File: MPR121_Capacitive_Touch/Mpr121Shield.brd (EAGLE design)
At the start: 39 x 28.7 mm, 13 parts

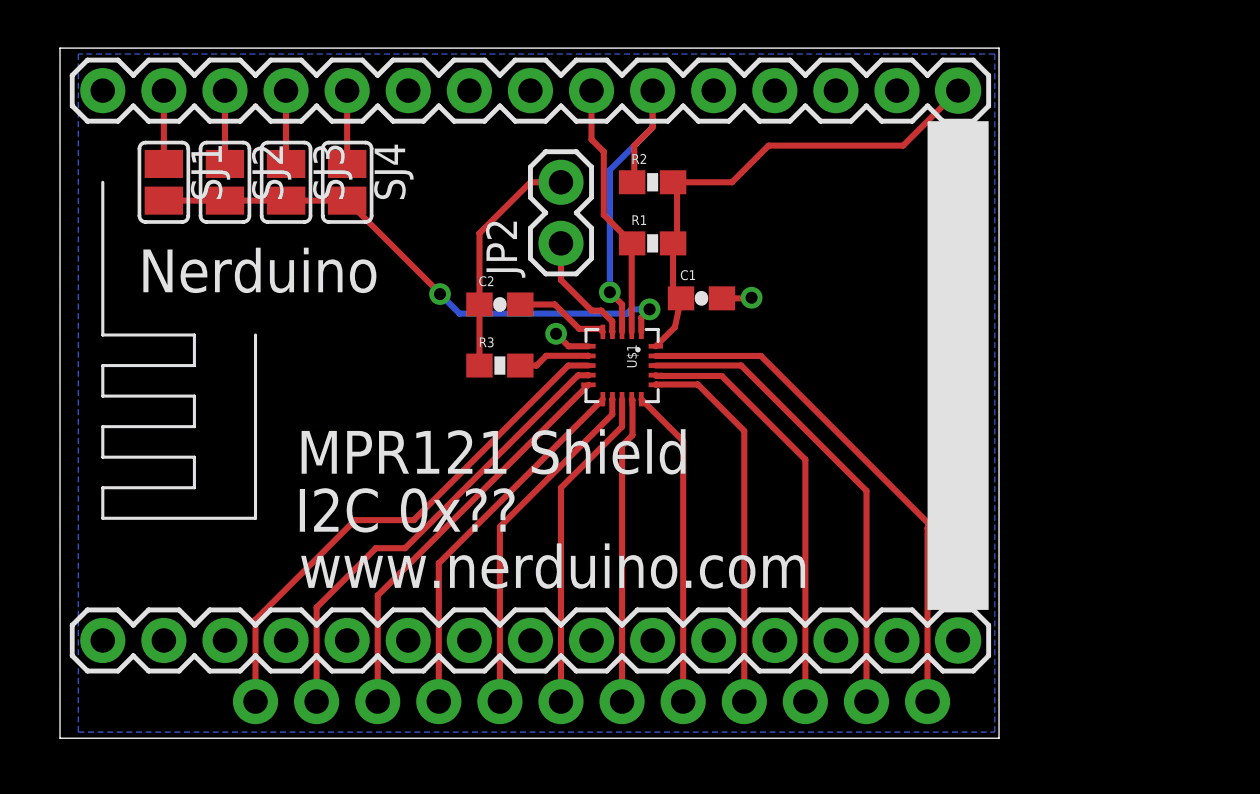
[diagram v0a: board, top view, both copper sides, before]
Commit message: Added OLED Shield Added LiPo Battery Charger Shield Updated outlines of all shields to match the cutout of the nodemcu board
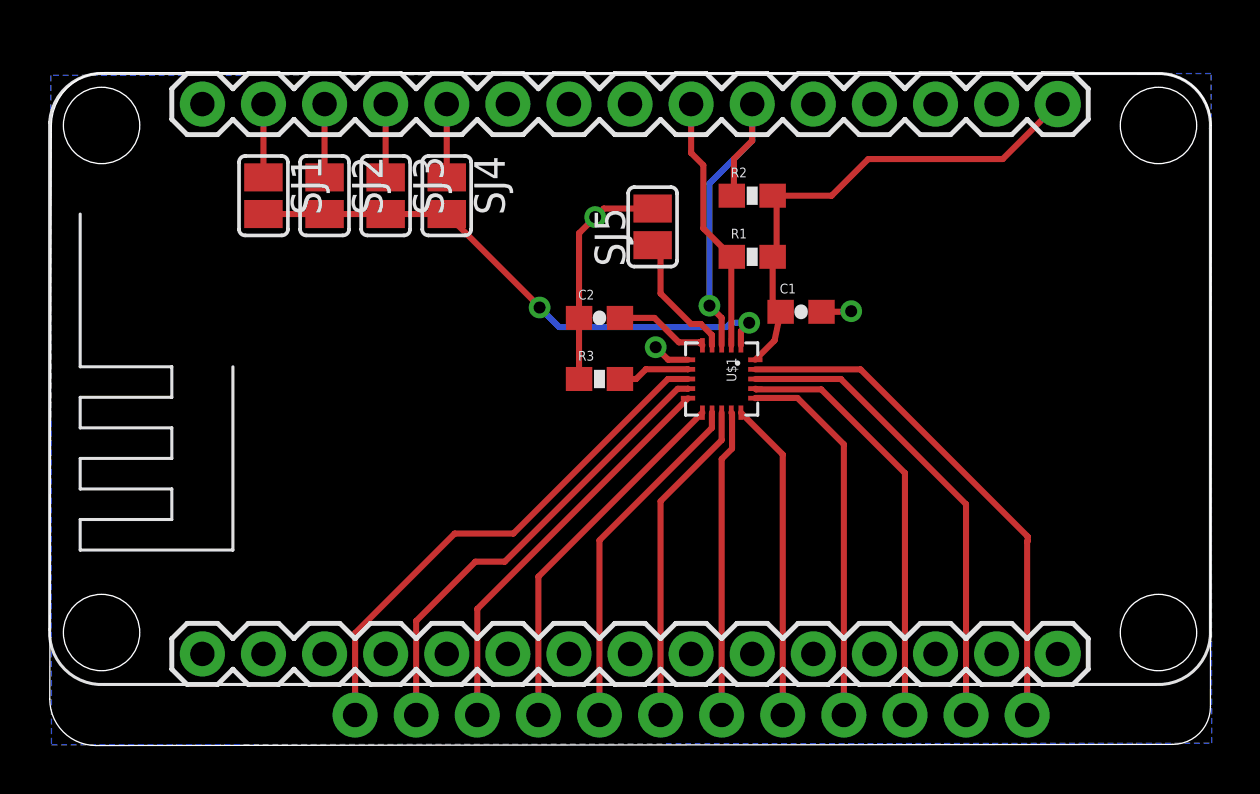
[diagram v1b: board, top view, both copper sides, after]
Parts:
- removed JP2: JP2, SparkFun:1X02
- added SJ5: (no value), jumper:SJ
- moved C1 4.18 mm to (31.6, 18.7)
- moved C2 4.18 mm to (23.2, 18.5)
- moved JP3 4.18 mm to (41.0, 1.98)
- moved R1 4.18 mm to (29.5, 21.0)
- moved R2 4.18 mm to (29.5, 23.6)
- moved R3 4.18 mm to (23.2, 16.0)
- moved SJ1 4.18 mm to (9.22, 23.6)
- moved SJ3 4.18 mm to (14.3, 23.6)
- moved SJ4 4.18 mm to (16.8, 23.6)
- moved U$1 4.18 mm to (28.3, 16.0)
- moved U$2 4.18 mm to (24.5, 9.60)
- moved SJ2 4.18 mm to (11.8, 23.6)
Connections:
- net GND: now also SJ5.2; no longer JP2.2, U$2.7
- net N$18: now also SJ5.1; no longer JP2.1
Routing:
- net N$18: track 4.80 -> 5.42 mm
- net GND: track 13.0 -> 13.1 mm, vias 2 -> 3
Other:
- board size 39 x 28.7 mm -> 48.3 x 28 mm
- board text added: "NERDUINO MPR121 Shield I2C 0x?? www.nerduino.com"
- board text removed: "I2C 0x??"
- board text removed: "MPR121 Shield"
- board text removed: "Nerduino"
- board text removed: "www.nerduino.com"

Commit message: Updated the i2c pins to all shields to use d11/d12  as these pins will have dual use with the upcoming wifimcu Added FM24W256  Fram shield Added X95840 Digital potentiometer Shield Added AD5696 DAC Shield
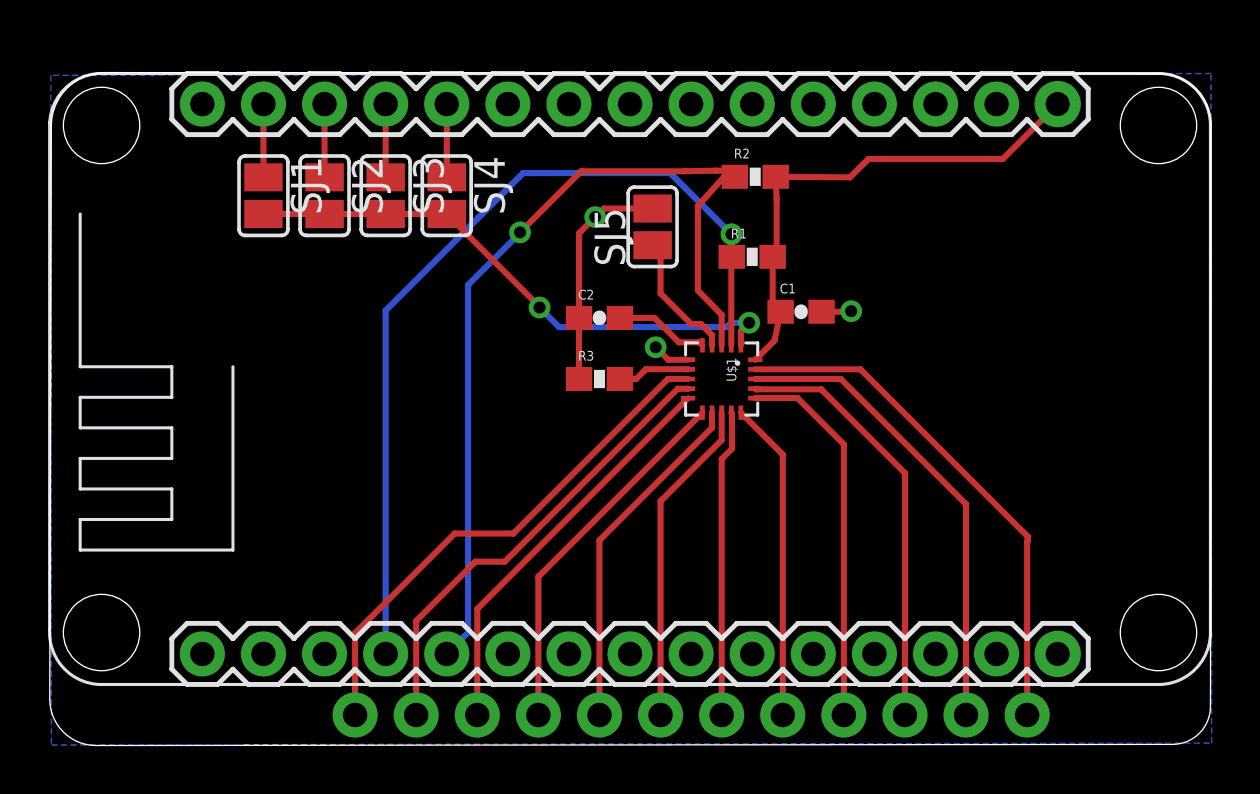
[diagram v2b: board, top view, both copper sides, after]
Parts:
- moved R2 0.80 mm to (29.7, 24.4)
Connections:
- net GND: no longer U$2.24
- net N$2: now also U$2.4; no longer U$2.22
- net N$4: now also U$2.5; no longer U$2.21
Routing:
- net N$2: track 10.7 -> 37.0 mm, vias 0 -> 1
- net N$4: track 15.1 -> 37.1 mm
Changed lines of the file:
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@@
 <element name="JP3" library="SparkFun-Connectors" package="1X12_NO_SILK" value="" x="40.9702" y="1.9812" rot="R180"/>
 <element name="R1" library="SparkFun" package="0603-RES" value="4.7K" x="29.5402" y="21.0312"/>
-<element name="R2" library="SparkFun" package="0603-RES" value="4.7K" x="29.5402" y="23.5712"/>
+<element name="R2" library="SparkFun" package="0603-RES" value="4.7K" x="29.6672" y="24.3586"/>
 <element name="R3" library="SparkFun" package="0603-RES" value="4.7K" x="23.1902" y="15.9512"/>
 <element name="SJ1" library="jumper" package="SJ" value="" x="9.2202" y="23.5712" rot="R270"/>
@@
 <signal name="GND">
 <contactref element="C1" pad="2"/>
-<contactref element="U$2" pad="24"/>
 <contactref element="U$2" pad="17"/>
 <contactref element="U$2" pad="14"/>
@@
 <wire x1="30.3902" y1="21.1192" x2="30.5562" y2="21.2852" width="0.254" layer="1"/>
 <wire x1="30.5562" y1="21.2852" x2="30.5562" y2="23.4052" width="0.254" layer="1"/>
-<wire x1="30.5562" y1="23.4052" x2="30.3902" y2="23.5712" width="0.254" layer="1"/>
-<wire x1="30.3902" y1="23.5712" x2="32.8422" y2="23.5712" width="0.254" layer="1"/>
-<wire x1="32.8422" y1="23.5712" x2="34.3662" y2="25.0952" width="0.254" layer="1"/>
+<wire x1="30.5562" y1="23.4052" x2="30.5172" y2="24.3586" width="0.254" layer="1"/>
+<wire x1="30.5172" y1="24.3586" x2="33.6042" y2="24.3332" width="0.254" layer="1"/>
+<wire x1="33.6042" y1="24.3332" x2="34.3662" y2="25.0952" width="0.254" layer="1"/>
 <wire x1="34.3662" y1="25.0952" x2="39.9542" y2="25.0952" width="0.254" layer="1"/>
 <wire x1="39.9542" y1="25.0952" x2="42.2402" y2="27.3812" width="0.254" layer="1"/>
@@
 </signal>
 <signal name="N$2">
-<contactref element="U$2" pad="22"/>
 <contactref element="U$1" pad="2"/>
 <contactref element="R1" pad="1"/>
-<wire x1="27.0002" y1="27.3812" x2="27.0002" y2="25.3492" width="0.254" layer="1"/>
-<wire x1="27.0002" y1="25.3492" x2="27.5082" y2="24.8412" width="0.254" layer="1"/>
-<wire x1="27.5082" y1="24.8412" x2="27.5082" y2="22.2132" width="0.254" layer="1"/>
-<wire x1="27.5082" y1="22.2132" x2="28.6902" y2="21.0312" width="0.254" layer="1"/>
-<wire x1="28.6702" y1="17.3512" x2="28.6702" y2="21.0112" width="0.254" layer="1"/>
+<wire x1="28.6702" y1="17.3512" x2="28.6702" y2="20.7264" width="0.254" layer="1"/>
+<wire x1="28.6702" y1="20.7264" x2="28.6702" y2="21.0112" width="0.254" layer="1"/>
 <wire x1="28.6702" y1="21.0112" x2="28.6902" y2="21.0312" width="0.254" layer="1"/>
+<contactref element="U$2" pad="4"/>
+<wire x1="14.3002" y1="4.5212" x2="14.3002" y2="18.796" width="0.254" layer="16"/>
+<wire x1="14.3002" y1="18.796" x2="20.0152" y2="24.511" width="0.254" layer="16"/>
+<wire x1="20.0152" y1="24.511" x2="26.1366" y2="24.511" width="0.254" layer="16"/>
+<wire x1="26.1366" y1="24.511" x2="28.6766" y2="21.971" width="0.254" layer="16"/>
+<via x="28.6766" y="21.971" extent="1-16" drill="0.5"/>
+<wire x1="28.6766" y1="21.971" x2="28.6766" y2="20.7328" width="0.254" layer="1"/>
+<wire x1="28.6766" y1="20.7328" x2="28.6702" y2="20.7264" width="0.254" layer="1"/>
 </signal>
 <signal name="N$4">
-<contactref element="U$2" pad="21"/>
 <contactref element="U$1" pad="3"/>
 <contactref element="R2" pad="1"/>
-<wire x1="29.5402" y1="27.3812" x2="29.5402" y2="25.8572" width="0.254" layer="1"/>
-<wire x1="29.5402" y1="25.8572" x2="28.7782" y2="25.0952" width="0.254" layer="1"/>
-<wire x1="28.7782" y1="25.0952" x2="28.7782" y2="23.6592" width="0.254" layer="1"/>
-<wire x1="28.7782" y1="23.6592" x2="28.6902" y2="23.5712" width="0.254" layer="1"/>
-<wire x1="28.2702" y1="17.3512" x2="28.2702" y2="18.4912" width="0.254" layer="1"/>
-<wire x1="28.2702" y1="18.4912" x2="27.7622" y2="18.9992" width="0.254" layer="1"/>
-<via x="27.7622" y="18.9992" extent="1-16" drill="0.5"/>
-<wire x1="27.7622" y1="18.9992" x2="27.7622" y2="24.0792" width="0.254" layer="16"/>
-<wire x1="27.7622" y1="24.0792" x2="29.5402" y2="25.8572" width="0.254" layer="16"/>
-<wire x1="29.5402" y1="25.8572" x2="29.5402" y2="27.3812" width="0.254" layer="16"/>
+<wire x1="28.8544" y1="24.3958" x2="28.8172" y2="24.3586" width="0.254" layer="1"/>
+<contactref element="U$2" pad="5"/>
+<wire x1="28.8172" y1="24.3586" x2="28.6004" y2="24.6126" width="0.254" layer="1"/>
+<wire x1="28.6004" y1="24.6126" x2="28.0416" y2="24.6126" width="0.254" layer="1"/>
+<wire x1="28.0416" y1="24.6126" x2="26.7462" y2="24.5872" width="0.254" layer="1"/>
+<wire x1="26.7462" y1="24.5872" x2="22.4282" y2="24.5872" width="0.254" layer="1"/>
+<wire x1="22.4282" y1="24.5872" x2="19.8882" y2="22.0472" width="0.254" layer="1"/>
+<via x="19.8882" y="22.0472" extent="1-16" drill="0.5"/>
+<wire x1="19.8882" y1="22.0472" x2="19.8882" y2="22.0218" width="0.254" layer="16"/>
+<wire x1="19.8882" y1="22.0218" x2="17.7292" y2="19.8628" width="0.254" layer="16"/>
+<wire x1="17.7292" y1="19.8628" x2="17.7292" y2="5.4102" width="0.254" layer="16"/>
+<wire x1="17.7292" y1="5.4102" x2="16.8402" y2="4.5212" width="0.254" layer="16"/>
+<wire x1="28.2702" y1="17.3512" x2="28.2702" y2="18.6182" width="0.254" layer="1"/>
+<wire x1="28.2702" y1="18.6182" x2="27.2796" y2="19.6342" width="0.254" layer="1"/>
+<wire x1="27.2796" y1="19.6342" x2="27.2796" y2="23.1394" width="0.254" layer="1"/>
+<wire x1="27.2796" y1="23.1394" x2="28.6004" y2="24.6126" width="0.254" layer="1"/>
 </signal>
 <signal name="N$1">
